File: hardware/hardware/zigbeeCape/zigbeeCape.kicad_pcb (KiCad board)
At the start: 4 copper layers, 63.5 x 54.6 mm, 75 parts, among them J1 Conn_ARM_JTAG_SWD_10, SW1 SW_MEC_5E, SW2 SW_MEC_5E, SW3 SW_MEC_5E, SW4 SW_MEC_5E, SW5 SW_MEC_5E, U1 CC1352R, U2 0.8Ghz_and_2.4GHz_Filter, U3 SMA_Antenna, U4 BeagleBone_P8, U5 BeagleBone_P9, Y1 32.768kHz, Y2 48MHz

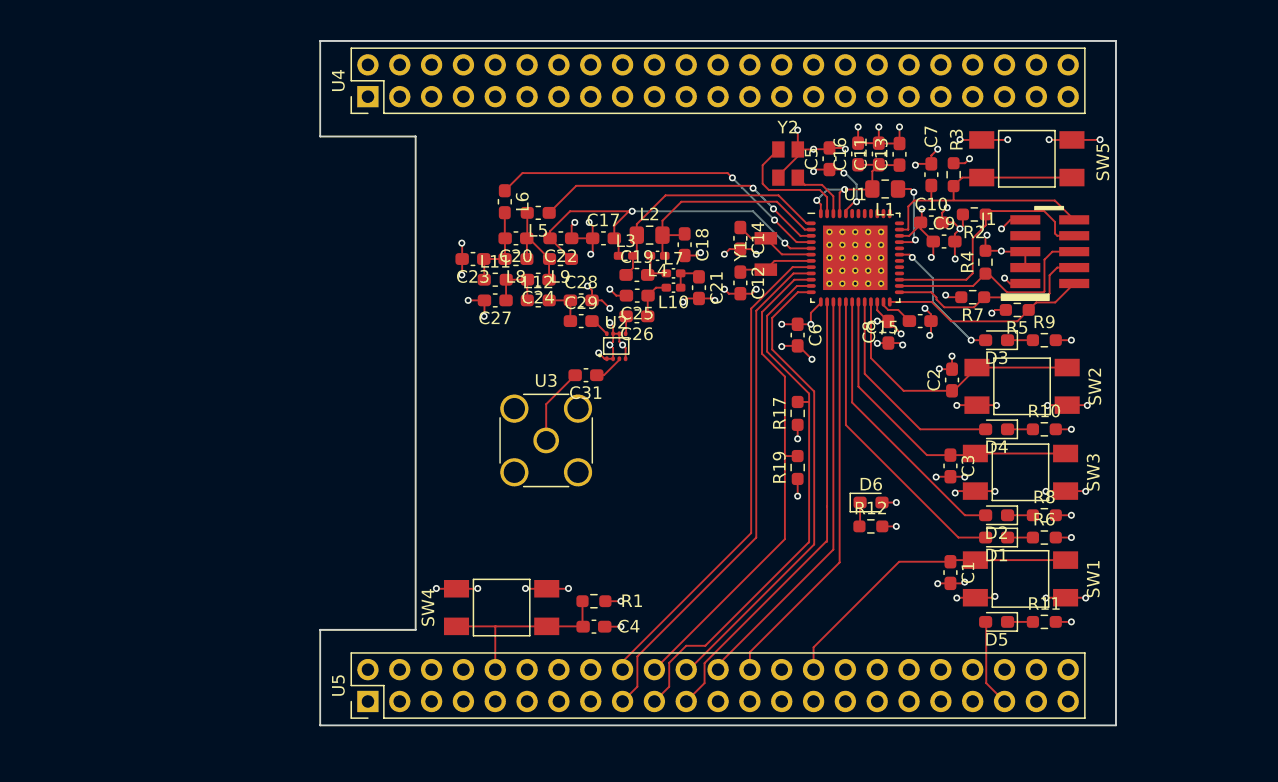
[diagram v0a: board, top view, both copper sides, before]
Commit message: Added Layout title and adjusted part refs
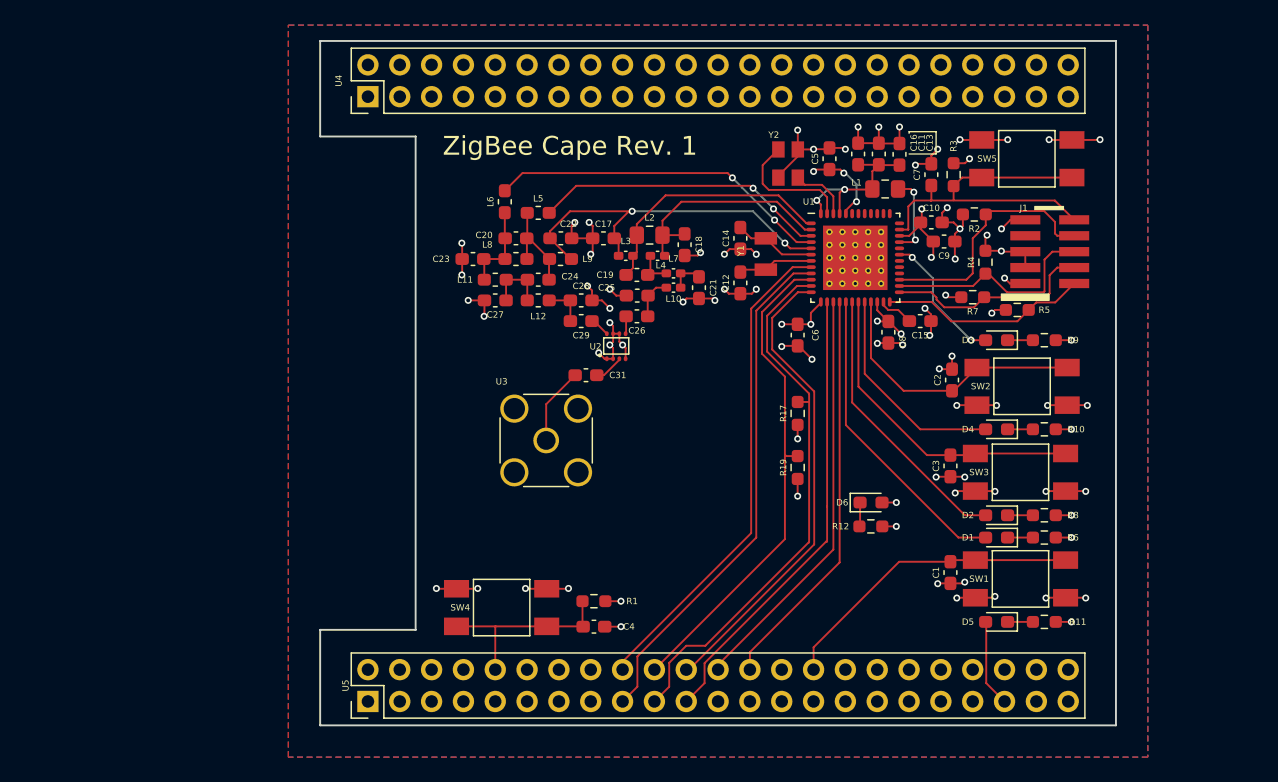
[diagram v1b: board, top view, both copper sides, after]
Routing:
- added copper zone on B.Cu, net GND
- added copper zone on F.Cu, net GND
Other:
- board text added: "ZigBee Cape Rev. 1"

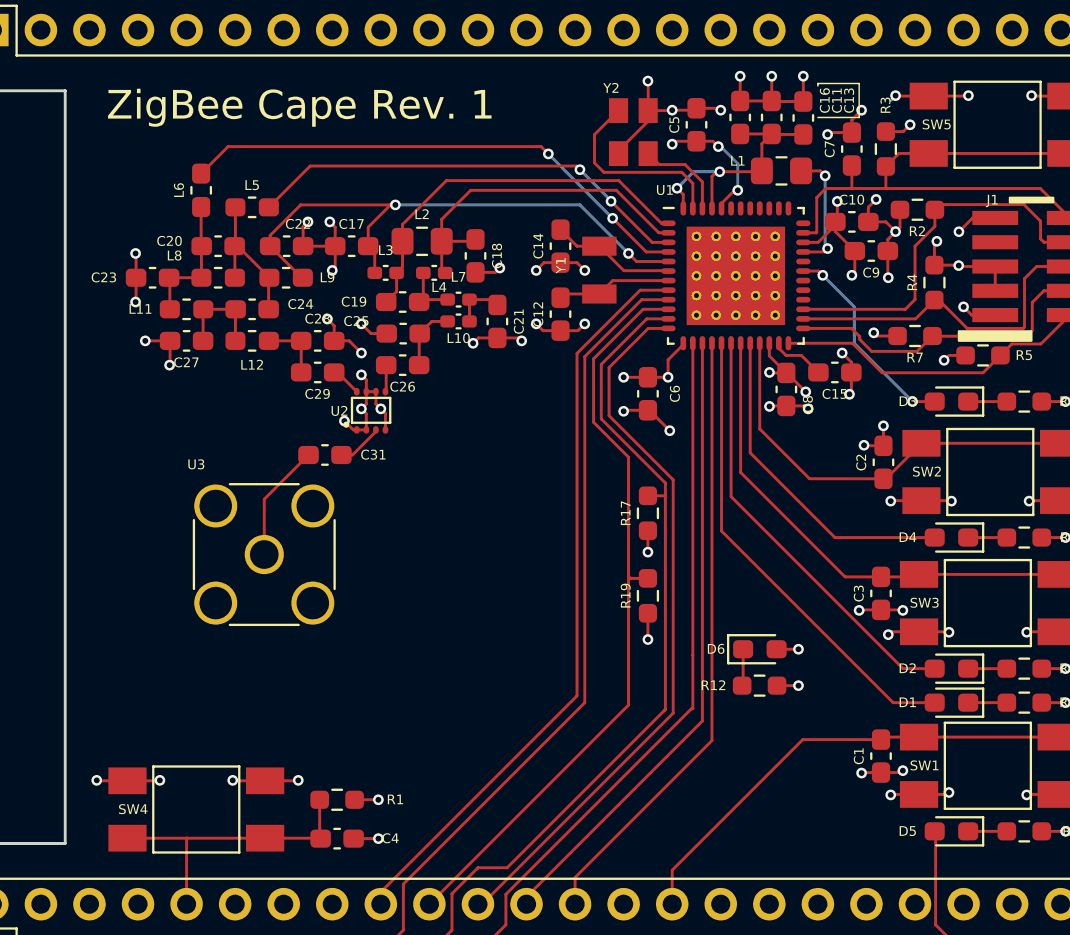
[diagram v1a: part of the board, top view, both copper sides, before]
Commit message: Post layout review 1 changes
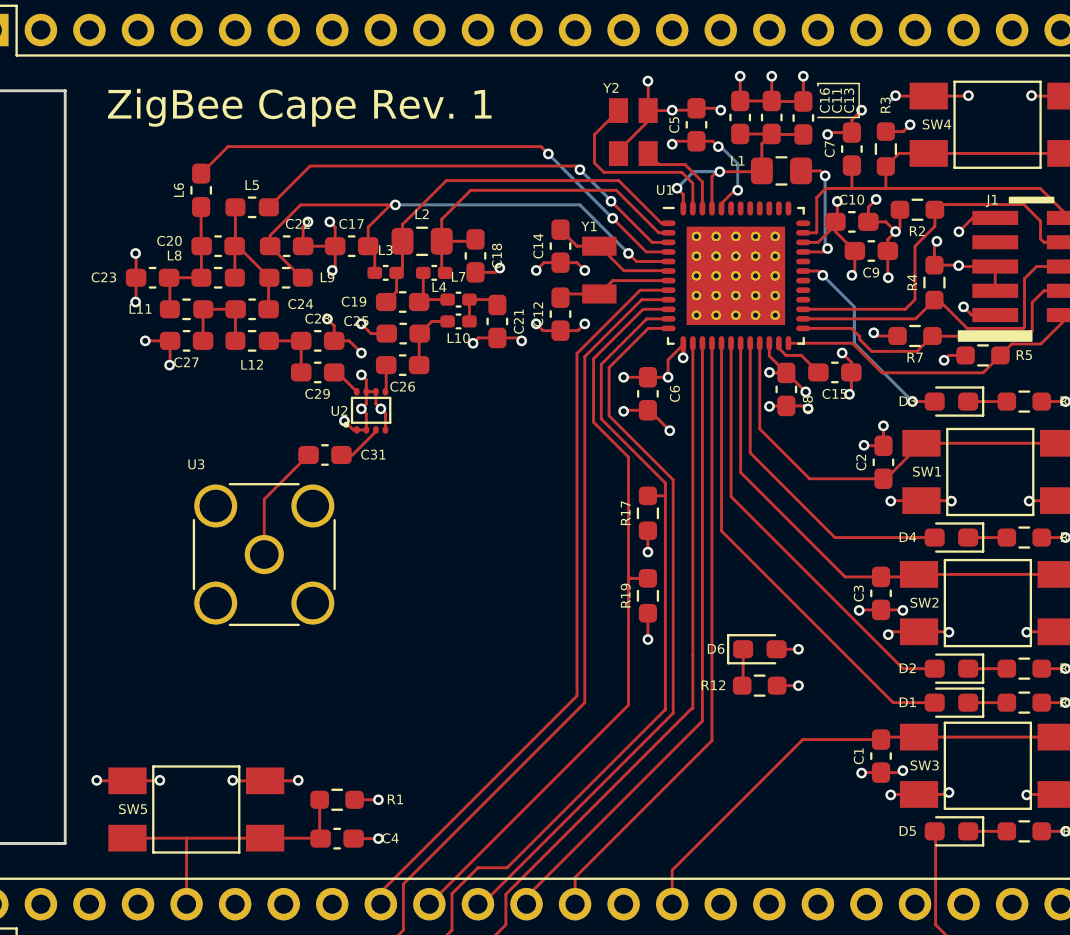
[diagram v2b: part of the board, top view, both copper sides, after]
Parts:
- renumbered SW2 to SW1, SW3 to SW2, SW1 to SW3, SW5 to SW4, SW4 to SW5
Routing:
- net +3V3: track 30.0 -> 30.8 mm, vias 15 -> 16

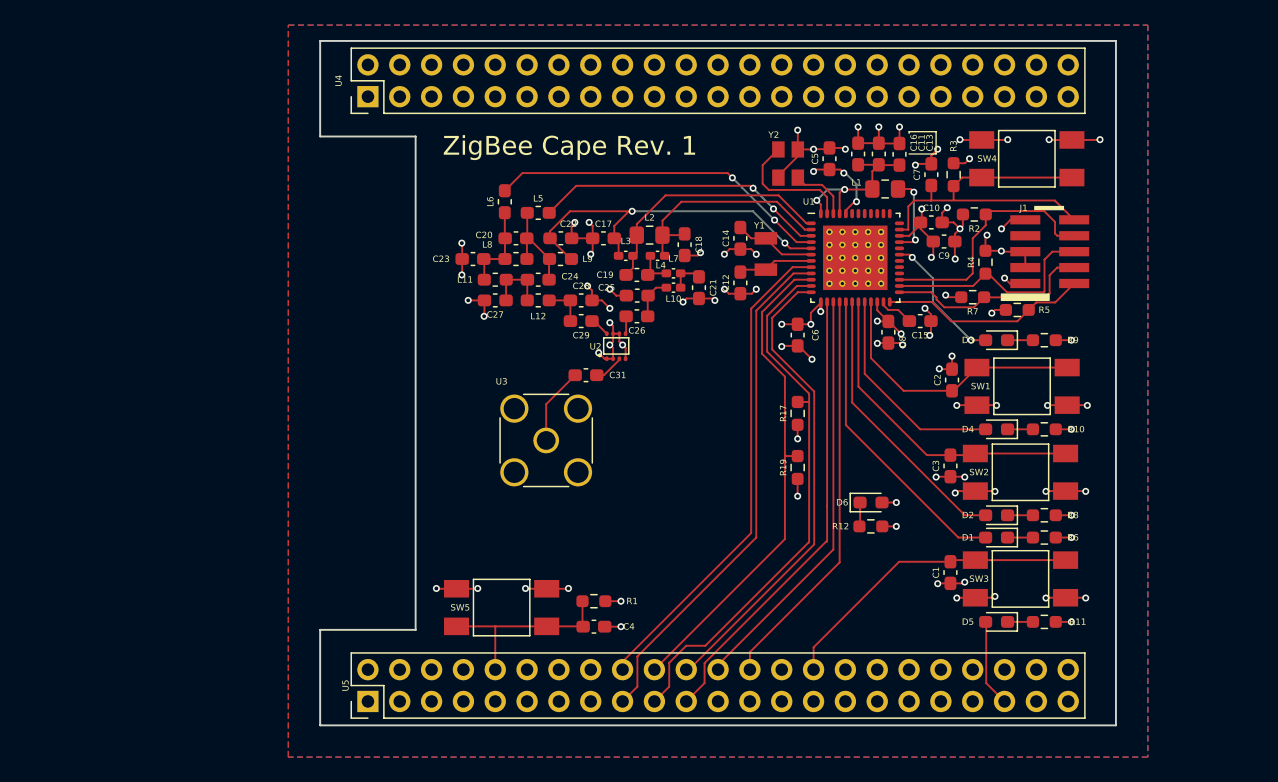
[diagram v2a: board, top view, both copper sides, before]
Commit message: Add ViaStitch-0.6 part, started stitching gnd planes
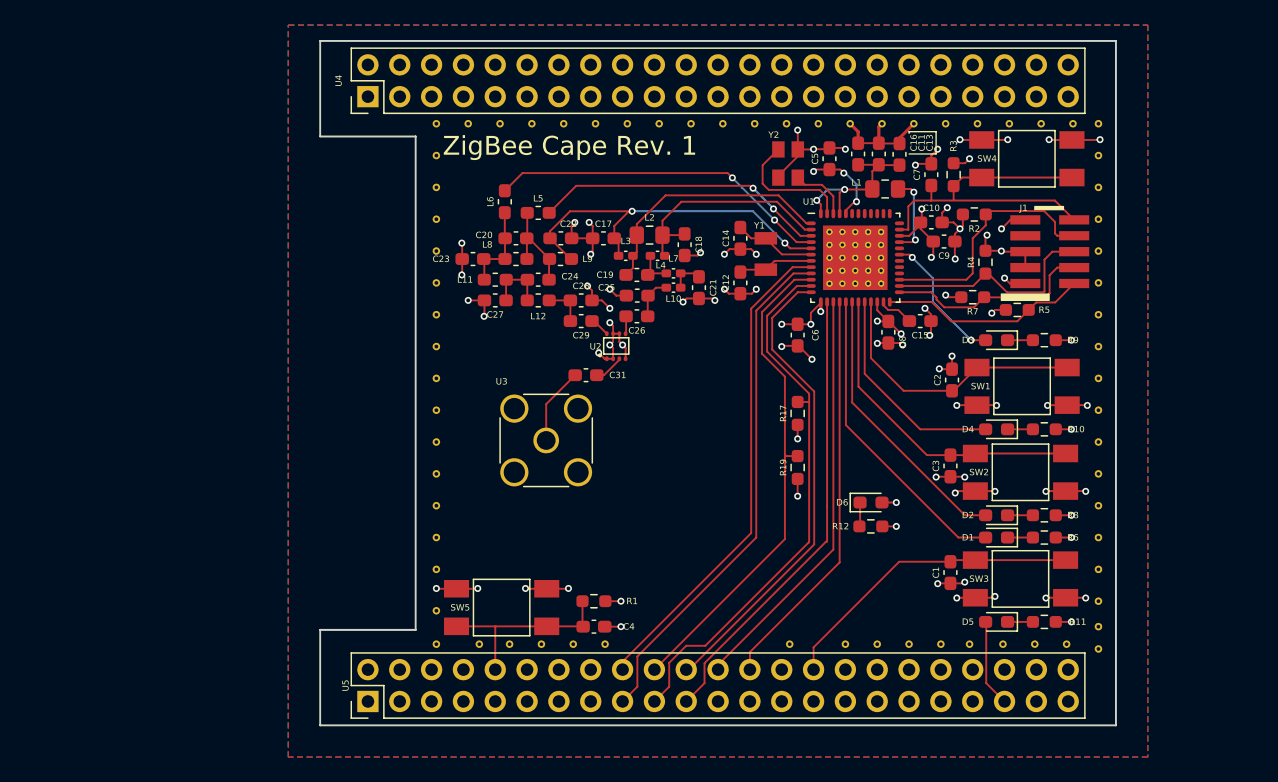
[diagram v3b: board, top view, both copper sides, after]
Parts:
- added REF**: ViaStitch-0.6mm, zigbeeCape:ViaStitch-0.6mm, F.Cu at (59.6, -7.49)
- added REF**: ViaStitch-0.6mm, zigbeeCape:ViaStitch-0.6mm, F.Cu at (22.7, -7.49)
- added REF**: ViaStitch-0.6mm, zigbeeCape:ViaStitch-0.6mm, F.Cu at (20.2, -7.49)
- added REF**: ViaStitch-0.6mm, zigbeeCape:ViaStitch-0.6mm, F.Cu at (17.7, -7.49)
- added REF**: ViaStitch-0.6mm, zigbeeCape:ViaStitch-0.6mm, F.Cu at (15.1, -7.49)
- added REF**: ViaStitch-0.6mm, zigbeeCape:ViaStitch-0.6mm, F.Cu at (12.7, -7.49)
- added REF**: ViaStitch-0.6mm, zigbeeCape:ViaStitch-0.6mm, F.Cu at (9.27, -48.0)
- added REF**: ViaStitch-0.6mm, zigbeeCape:ViaStitch-0.6mm, F.Cu at (9.27, -7.49)
- added REF**: ViaStitch-0.6mm, zigbeeCape:ViaStitch-0.6mm, F.Cu at (9.27, -9.14)
- added REF**: ViaStitch-0.6mm, zigbeeCape:ViaStitch-0.6mm, F.Cu at (9.27, -12.4)
- added REF**: ViaStitch-0.6mm, zigbeeCape:ViaStitch-0.6mm, F.Cu at (9.27, -15.0)
- added REF**: ViaStitch-0.6mm, zigbeeCape:ViaStitch-0.6mm, F.Cu at (57.0, -7.49)
- added REF**: ViaStitch-0.6mm, zigbeeCape:ViaStitch-0.6mm, F.Cu at (9.27, -17.5)
- added REF**: ViaStitch-0.6mm, zigbeeCape:ViaStitch-0.6mm, F.Cu at (9.27, -20.1)
- added REF**: ViaStitch-0.6mm, zigbeeCape:ViaStitch-0.6mm, F.Cu at (9.27, -22.6)
- added REF**: ViaStitch-0.6mm, zigbeeCape:ViaStitch-0.6mm, F.Cu at (9.27, -25.1)
- added REF**: ViaStitch-0.6mm, zigbeeCape:ViaStitch-0.6mm, F.Cu at (9.27, -27.7)
- added REF**: ViaStitch-0.6mm, zigbeeCape:ViaStitch-0.6mm, F.Cu at (9.27, -30.2)
- added REF**: ViaStitch-0.6mm, zigbeeCape:ViaStitch-0.6mm, F.Cu at (9.27, -32.8)
- added REF**: ViaStitch-0.6mm, zigbeeCape:ViaStitch-0.6mm, F.Cu at (9.27, -35.3)
- added REF**: ViaStitch-0.6mm, zigbeeCape:ViaStitch-0.6mm, F.Cu at (9.27, -37.8)
- added REF**: ViaStitch-0.6mm, zigbeeCape:ViaStitch-0.6mm, F.Cu at (9.27, -40.4)
- added REF**: ViaStitch-0.6mm, zigbeeCape:ViaStitch-0.6mm, F.Cu at (54.5, -7.49)
- added REF**: ViaStitch-0.6mm, zigbeeCape:ViaStitch-0.6mm, F.Cu at (9.27, -42.9)
- added REF**: ViaStitch-0.6mm, zigbeeCape:ViaStitch-0.6mm, F.Cu at (9.27, -45.5)
- added REF**: ViaStitch-0.6mm, zigbeeCape:ViaStitch-0.6mm, F.Cu at (62.1, -6.10)
- added REF**: ViaStitch-0.6mm, zigbeeCape:ViaStitch-0.6mm, F.Cu at (62.1, -12.4)
- added REF**: ViaStitch-0.6mm, zigbeeCape:ViaStitch-0.6mm, F.Cu at (62.1, -7.87)
- added REF**: ViaStitch-0.6mm, zigbeeCape:ViaStitch-0.6mm, F.Cu at (62.1, -9.91)
- added REF**: ViaStitch-0.6mm, zigbeeCape:ViaStitch-0.6mm, F.Cu at (62.1, -15.0)
- added REF**: ViaStitch-0.6mm, zigbeeCape:ViaStitch-0.6mm, F.Cu at (62.1, -17.5)
- added REF**: ViaStitch-0.6mm, zigbeeCape:ViaStitch-0.6mm, F.Cu at (62.1, -20.1)
- added REF**: ViaStitch-0.6mm, zigbeeCape:ViaStitch-0.6mm, F.Cu at (62.1, -22.6)
- added REF**: ViaStitch-0.6mm, zigbeeCape:ViaStitch-0.6mm, F.Cu at (51.8, -7.49)
- added REF**: ViaStitch-0.6mm, zigbeeCape:ViaStitch-0.6mm, F.Cu at (62.1, -25.1)
- added REF**: ViaStitch-0.6mm, zigbeeCape:ViaStitch-0.6mm, F.Cu at (62.1, -27.7)
- added REF**: ViaStitch-0.6mm, zigbeeCape:ViaStitch-0.6mm, F.Cu at (62.1, -30.2)
- added REF**: ViaStitch-0.6mm, zigbeeCape:ViaStitch-0.6mm, F.Cu at (62.1, -32.8)
- added REF**: ViaStitch-0.6mm, zigbeeCape:ViaStitch-0.6mm, F.Cu at (62.1, -35.3)
- added REF**: ViaStitch-0.6mm, zigbeeCape:ViaStitch-0.6mm, F.Cu at (62.1, -37.8)
- added REF**: ViaStitch-0.6mm, zigbeeCape:ViaStitch-0.6mm, F.Cu at (62.1, -40.4)
- added REF**: ViaStitch-0.6mm, zigbeeCape:ViaStitch-0.6mm, F.Cu at (62.1, -42.9)
- added REF**: ViaStitch-0.6mm, zigbeeCape:ViaStitch-0.6mm, F.Cu at (62.1, -45.5)
- added REF**: ViaStitch-0.6mm, zigbeeCape:ViaStitch-0.6mm, F.Cu at (62.1, -48.0)
- added REF**: ViaStitch-0.6mm, zigbeeCape:ViaStitch-0.6mm, F.Cu at (49.5, -7.49)
- added REF**: ViaStitch-0.6mm, zigbeeCape:ViaStitch-0.6mm, F.Cu at (55.0, -48.0)
- added REF**: ViaStitch-0.6mm, zigbeeCape:ViaStitch-0.6mm, F.Cu at (60.1, -48.0)
- added REF**: ViaStitch-0.6mm, zigbeeCape:ViaStitch-0.6mm, F.Cu at (57.5, -48.0)
- added REF**: ViaStitch-0.6mm, zigbeeCape:ViaStitch-0.6mm, F.Cu at (52.5, -48.0)
- added REF**: ViaStitch-0.6mm, zigbeeCape:ViaStitch-0.6mm, F.Cu at (49.9, -48.0)
- added REF**: ViaStitch-0.6mm, zigbeeCape:ViaStitch-0.6mm, F.Cu at (47.4, -48.0)
- added REF**: ViaStitch-0.6mm, zigbeeCape:ViaStitch-0.6mm, F.Cu at (44.8, -48.0)
- added REF**: ViaStitch-0.6mm, zigbeeCape:ViaStitch-0.6mm, F.Cu at (42.3, -48.0)
- added REF**: ViaStitch-0.6mm, zigbeeCape:ViaStitch-0.6mm, F.Cu at (39.8, -48.0)
- added REF**: ViaStitch-0.6mm, zigbeeCape:ViaStitch-0.6mm, F.Cu at (37.2, -48.0)
- added REF**: ViaStitch-0.6mm, zigbeeCape:ViaStitch-0.6mm, F.Cu at (47.0, -7.49)
- added REF**: ViaStitch-0.6mm, zigbeeCape:ViaStitch-0.6mm, F.Cu at (34.7, -48.0)
- added REF**: ViaStitch-0.6mm, zigbeeCape:ViaStitch-0.6mm, F.Cu at (32.1, -48.0)
- added REF**: ViaStitch-0.6mm, zigbeeCape:ViaStitch-0.6mm, F.Cu at (29.6, -48.0)
- added REF**: ViaStitch-0.6mm, zigbeeCape:ViaStitch-0.6mm, F.Cu at (27.1, -48.0)
- added REF**: ViaStitch-0.6mm, zigbeeCape:ViaStitch-0.6mm, F.Cu at (24.5, -48.0)
- added REF**: ViaStitch-0.6mm, zigbeeCape:ViaStitch-0.6mm, F.Cu at (22.0, -48.0)
- added REF**: ViaStitch-0.6mm, zigbeeCape:ViaStitch-0.6mm, F.Cu at (19.4, -48.0)
- added REF**: ViaStitch-0.6mm, zigbeeCape:ViaStitch-0.6mm, F.Cu at (16.9, -48.0)
- added REF**: ViaStitch-0.6mm, zigbeeCape:ViaStitch-0.6mm, F.Cu at (14.4, -48.0)
- added REF**: ViaStitch-0.6mm, zigbeeCape:ViaStitch-0.6mm, F.Cu at (11.8, -48.0)
- added REF**: ViaStitch-0.6mm, zigbeeCape:ViaStitch-0.6mm, F.Cu at (44.5, -7.49)
- added REF**: ViaStitch-0.6mm, zigbeeCape:ViaStitch-0.6mm, F.Cu at (41.9, -7.49)
- added REF**: ViaStitch-0.6mm, zigbeeCape:ViaStitch-0.6mm, F.Cu at (37.5, -7.49)
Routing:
- net GND: track 125.0 -> 126.6 mm, vias 76 -> 73
